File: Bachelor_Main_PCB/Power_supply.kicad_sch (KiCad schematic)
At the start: 11 parts, among them IC1 LD3985M18R, U9 LM73100RPWR

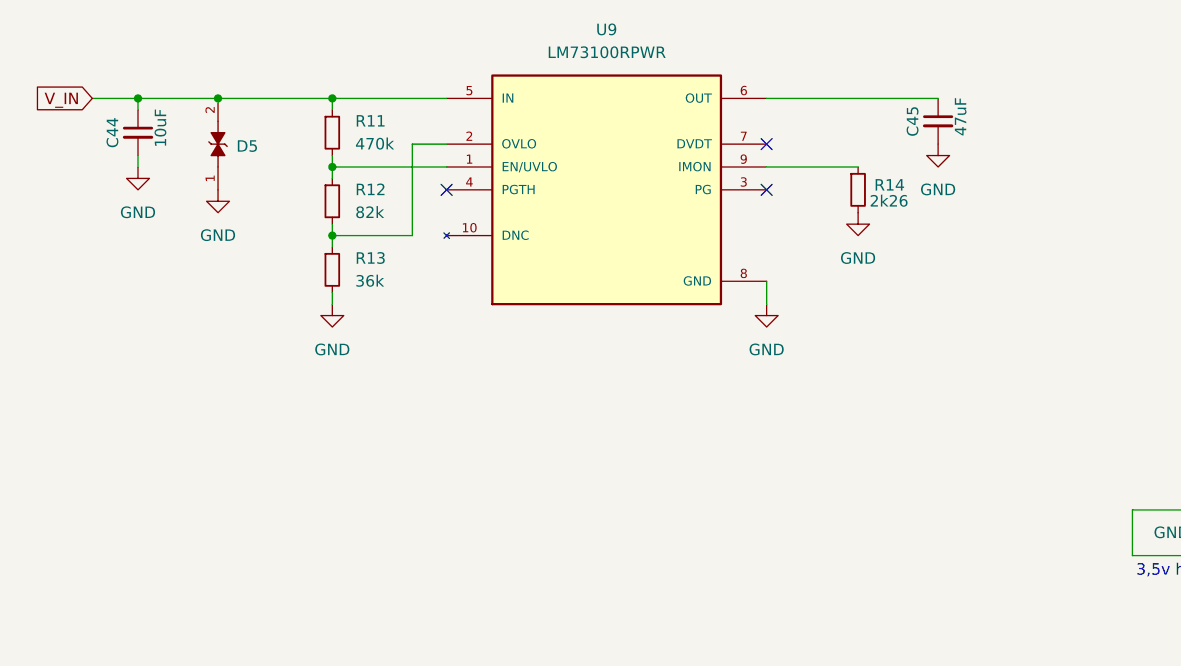
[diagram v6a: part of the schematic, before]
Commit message: Add Vin sampling and route V_IN and V_IMON to MCU sheet
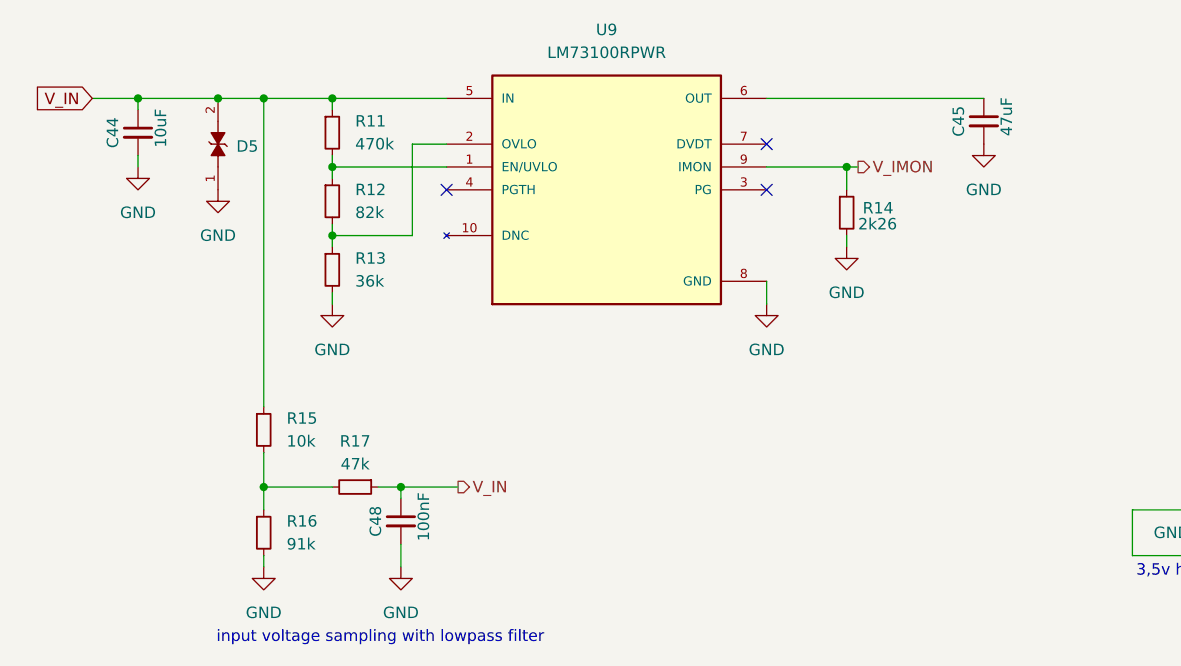
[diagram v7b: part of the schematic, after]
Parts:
- added C48: 100nF, Capacitor_SMD:C_0603_1608Metric, symbol Device:C_Small
- added R15: 10k, Resistor_SMD:R_0402_1005Metric, symbol Device:R_Small
- added R16: 91k, Resistor_SMD:R_0402_1005Metric, symbol Device:R_Small
- added R17: 47k, Resistor_SMD:R_0402_1005Metric, symbol Device:R_Small
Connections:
- net GND: now also C48.2, R16.2
- net V_IN: now also C48.1, R15.1, R17.1
- net V_IMON: now reaches R14.1, U9.9 (IMON)
- new net: R15.2, R16.1, R17.2
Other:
- note added: "input voltage sampling with lowpass filter"
- moved on the sheet: C45, R14

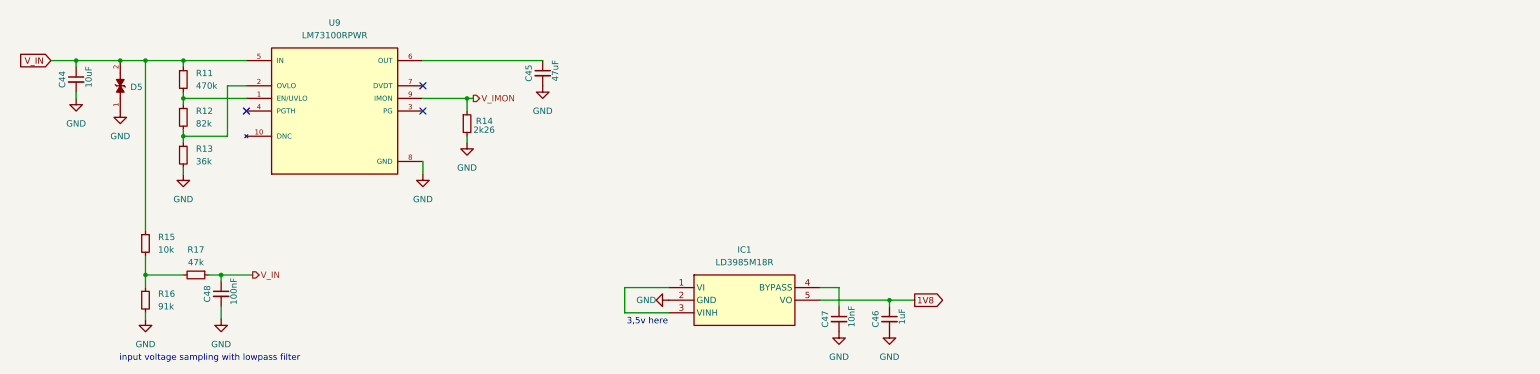
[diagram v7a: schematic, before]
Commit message: Add LMR51450 switch mode regulator.
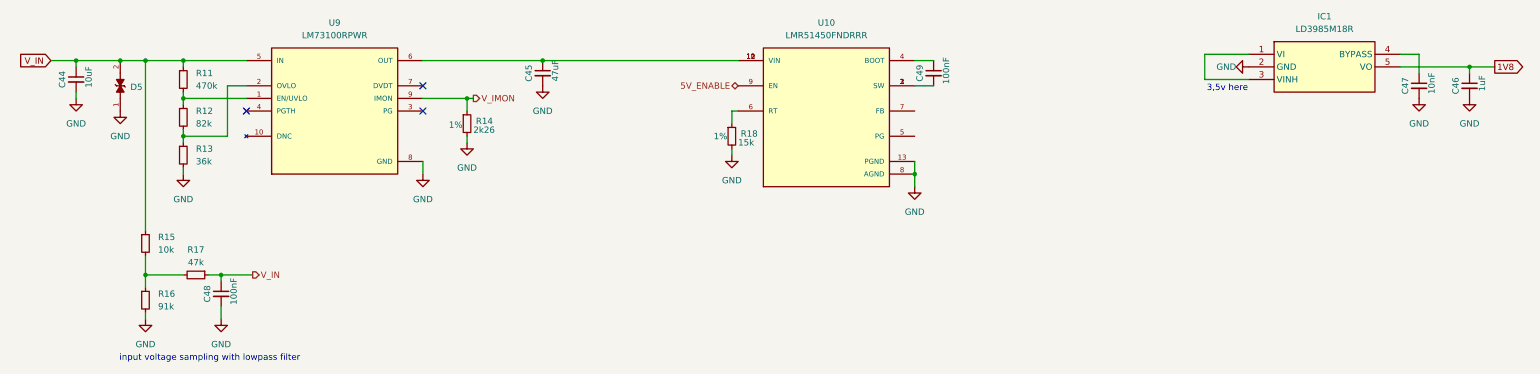
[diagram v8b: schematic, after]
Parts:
- added C49: 100nF, Capacitor_SMD:C_0603_1608Metric, symbol Device:C_Small
- added R18: 15k, Resistor_SMD:R_0402_1005Metric, symbol Device:R_Small
- added U10: LMR51450FNDRRR, LMR51450FNDRRR:CONV_LMR51450FNDRRR, symbol LMR51450FNDRRR:LMR51450FNDRRR
- R14: Tolerance (none) -> 1%
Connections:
- net GND: now also R18.2, U10.13 (PGND), U10.8 (AGND)
- net at C45.1, U9.6 (OUT): now also U10.10 (VIN), U10.11 (VIN), U10.12 (VIN)
- new net: R18.1, U10.6 (RT)
- new net: C49.2, U10.1 (SW), U10.2 (SW), U10.3 (SW)
- new net: C49.1, U10.4 (BOOT)
- new net 5V_ENABLE: U10.9 (EN)
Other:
- moved on the sheet: C46, C47, IC1
